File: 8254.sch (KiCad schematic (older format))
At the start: 4 parts, among them U18 PAL16L8, U19 8254

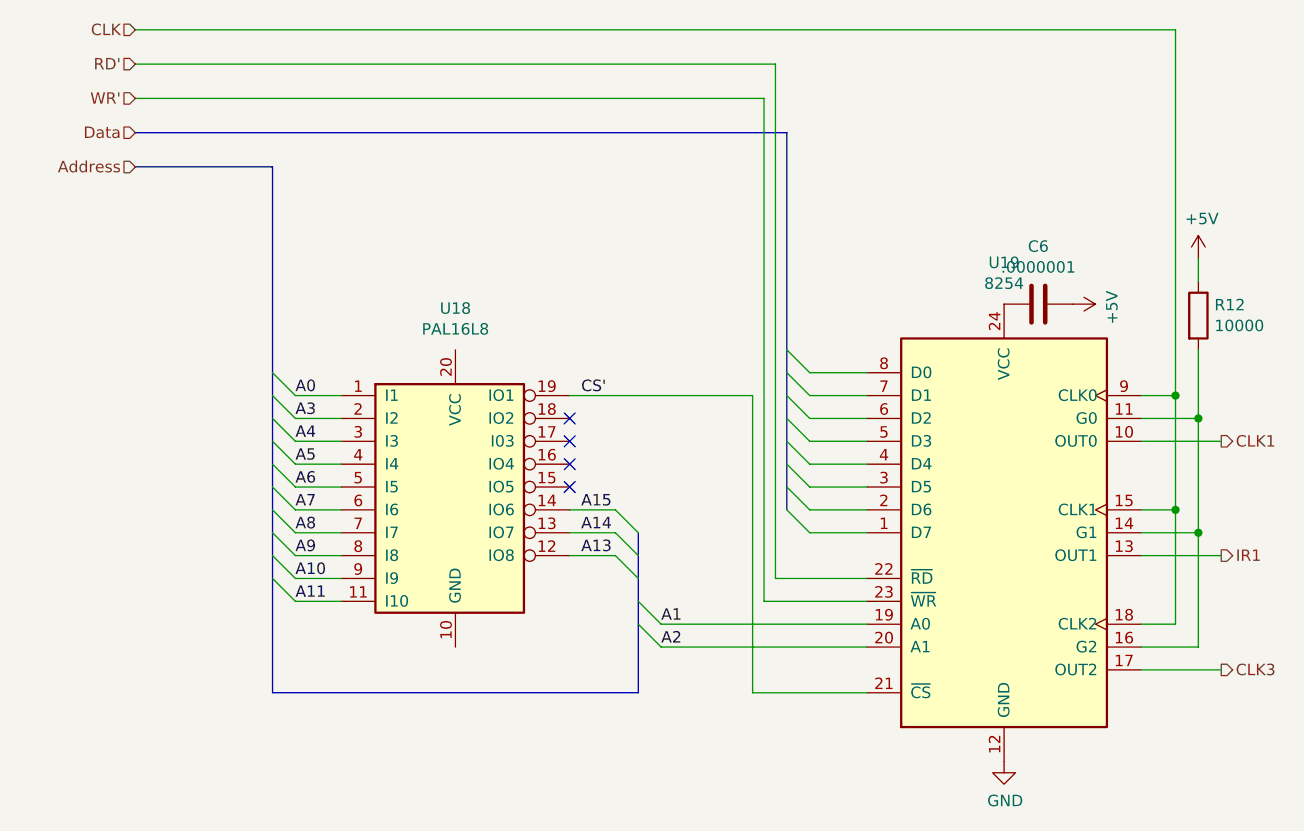
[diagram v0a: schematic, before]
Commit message: Integrated LCD.  Fixed issues with busses
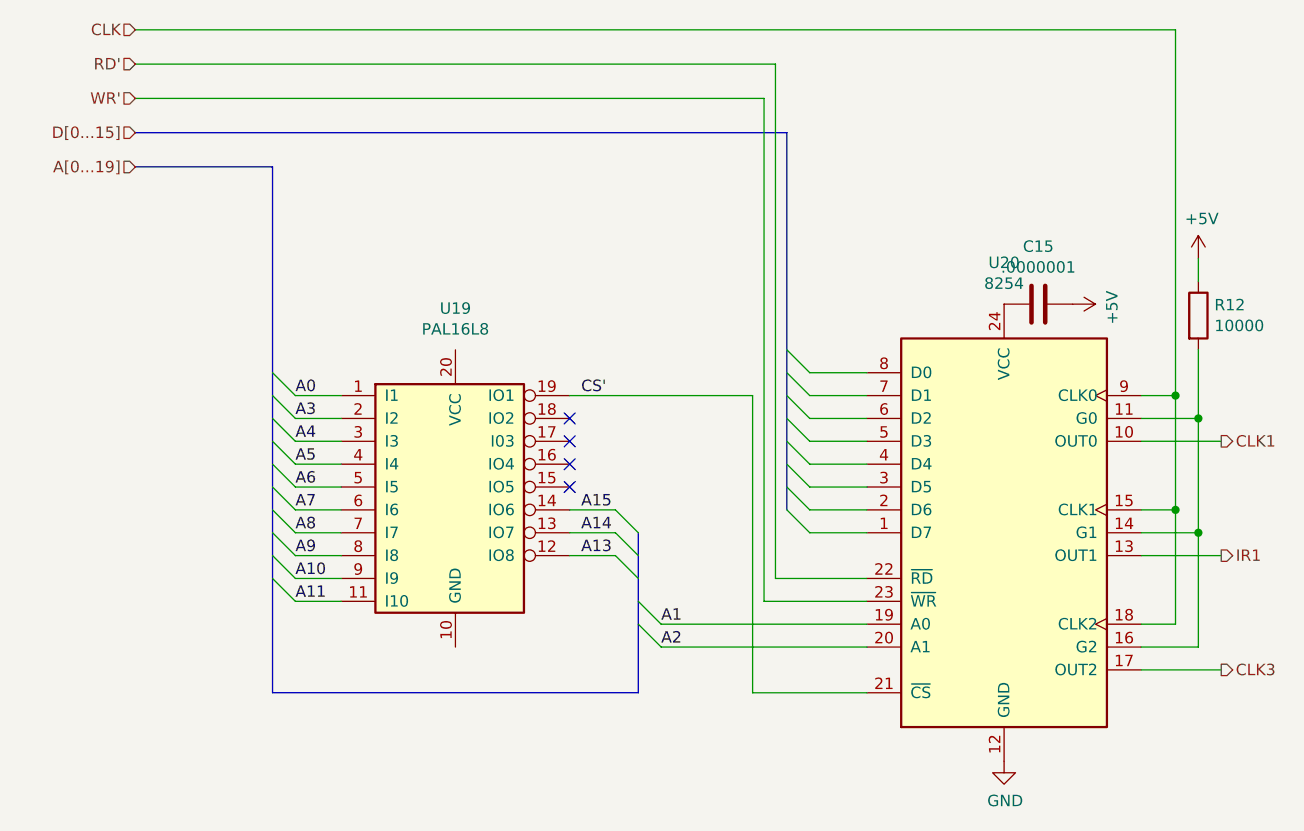
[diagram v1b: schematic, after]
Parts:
- renumbered C6 to C15, U18 to U19, U19 to U20
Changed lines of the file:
@@
 $Descr A4 11693 8268
 encoding utf-8
-Sheet 8 8
+Sheet 8 9
 Title ""
 Date ""
@@
 $EndDescr
 $Comp
-L Timer:8254 U19
+L Timer:8254 U20
 U 1 1 61B9DC78
 P 4950 3450
-F 0 "U19" H 4950 4631 50  0000 C CNN
+F 0 "U20" H 4950 4631 50  0000 C CNN
 F 1 "8254" H 4950 4540 50  0000 C CNN
 F 2 "Package_DIP:DIP-24_W15.24mm" H 5000 3700 50  0001 C CNN
@@
 $EndComp
 $Comp
-L power:+5V #PWR0112
+L power:+5V #PWR087
 U 1 1 61BA7924
 P 5250 2450
-F 0 "#PWR0112" H 5250 2300 50  0001 C CNN
+F 0 "#PWR087" H 5250 2300 50  0001 C CNN
 F 1 "+5V" H 5265 2623 50  0000 C CNN
 F 2 "" H 5250 2450 50  0001 C CNN
@@
 $EndComp
 $Comp
-L power:GND #PWR0113
+L power:GND #PWR086
 U 1 1 61BAD092
 P 4950 4450
-F 0 "#PWR0113" H 4950 4200 50  0001 C CNN
+F 0 "#PWR086" H 4950 4200 50  0001 C CNN
 F 1 "GND" H 4955 4277 50  0000 C CNN
 F 2 "" H 4950 4450 50  0001 C CNN
@@
 $EndComp
 $Comp
-L Logic_Programmable:PAL16L8 U18
+L Logic_Programmable:PAL16L8 U19
 U 1 1 61BB0CE0
 P 2550 3350
-F 0 "U18" H 2550 4231 50  0000 C CNN
+F 0 "U19" H 2550 4231 50  0000 C CNN
 F 1 "PAL16L8" H 2550 4140 50  0000 C CNN
 F 2 "" H 2550 3350 50  0001 C CNN
@@
 	1850 3750 2050 3750
 Text HLabel 1150 1700 0    50   Input ~ 0
-Data
+D[0...15]
 Text HLabel 1150 1850 0    50   Input ~ 0
-Address
+A[0...19]
 Wire Bus Line
 	1150 1700 4000 1700
@@
 	5700 2850 5700 3350
 $Comp
-L power:+5V #PWR0114
+L power:+5V #PWR088
 U 1 1 61BF17C5
 P 5800 2250
-F 0 "#PWR0114" H 5800 2100 50  0001 C CNN
+F 0 "#PWR088" H 5800 2100 50  0001 C CNN
 F 1 "+5V" H 5815 2423 50  0000 C CNN
 F 2 "" H 5800 2250 50  0001 C CNN
@@
 	3850 4150 4350 4150
 $Comp
-L Device:C C6
+L Device:C C15
 U 1 1 61C215F3
 P 5100 2450
-F 0 "C6" V 4848 2450 50  0000 C CNN
+F 0 "C15" V 4848 2450 50  0000 C CNN
 F 1 ".0000001" V 4939 2450 50  0000 C CNN
 F 2 "" H 5138 2300 50  0001 C CNN

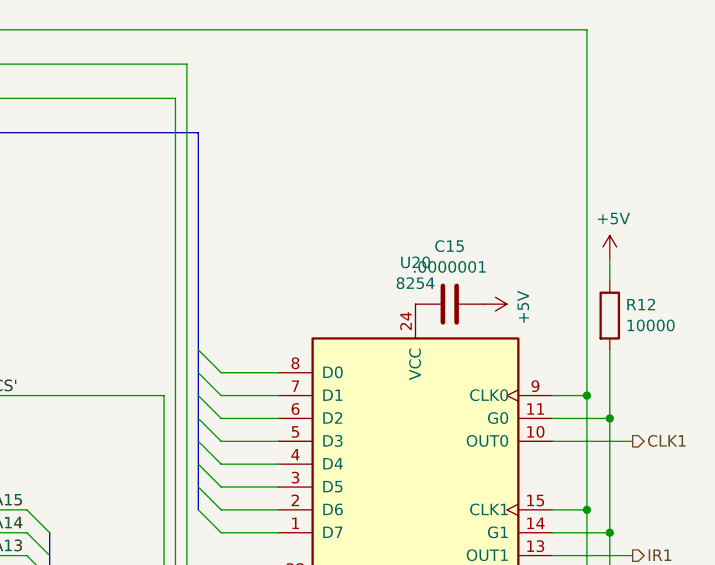
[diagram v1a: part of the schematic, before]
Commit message: All schematics present
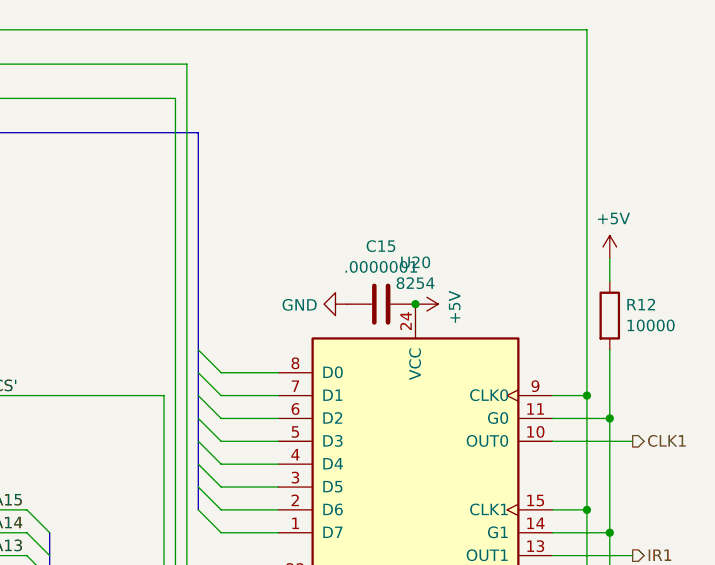
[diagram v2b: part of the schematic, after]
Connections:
- net +5V: now also U20.24 (VCC)
- net GND: now also C15.2
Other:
- moved on the sheet: C15
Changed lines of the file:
@@
 $Descr A4 11693 8268
 encoding utf-8
-Sheet 8 9
+Sheet 8 12
 Title ""
 Date ""
@@
 L power:+5V #PWR087
 U 1 1 61BA7924
-P 5250 2450
-F 0 "#PWR087" H 5250 2300 50  0001 C CNN
-F 1 "+5V" H 5265 2623 50  0000 C CNN
-F 2 "" H 5250 2450 50  0001 C CNN
-F 3 "" H 5250 2450 50  0001 C CNN
-	1    5250 2450
+P 4950 2450
+F 0 "#PWR087" H 4950 2300 50  0001 C CNN
+F 1 "+5V" H 4965 2623 50  0000 C CNN
+F 2 "" H 4950 2450 50  0001 C CNN
+F 3 "" H 4950 2450 50  0001 C CNN
+	1    4950 2450
 	0    1    1    0
 $EndComp
@@
 L Device:C C15
 U 1 1 61C215F3
-P 5100 2450
-F 0 "C15" V 4848 2450 50  0000 C CNN
-F 1 ".0000001" V 4939 2450 50  0000 C CNN
-F 2 "" H 5138 2300 50  0001 C CNN
-F 3 "~" H 5100 2450 50  0001 C CNN
-	1    5100 2450
+P 4800 2450
+F 0 "C15" V 4548 2450 50  0000 C CNN
+F 1 ".0000001" V 4639 2450 50  0000 C CNN
+F 2 "" H 4838 2300 50  0001 C CNN
+F 3 "~" H 4800 2450 50  0001 C CNN
+	1    4800 2450
 	0    1    1    0
 $EndComp
@@
 Wire Bus Line
 	1750 1850 1750 4150
+Connection ~ 4950 2450
+$Comp
+L power:GND #PWR0131
+U 1 1 61F867A8
+P 4650 2450
+F 0 "#PWR0131" H 4650 2200 50  0001 C CNN
+F 1 "GND" V 4655 2322 50  0000 R CNN
+F 2 "" H 4650 2450 50  0001 C CNN
+F 3 "" H 4650 2450 50  0001 C CNN
+	1    4650 2450
+	0    1    1    0
+$EndComp
 $EndSCHEMATC

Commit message: Started PCB
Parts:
- C35: renamed from C15; footprint (none) -> Capacitor_SMD:CP_Elec_3x5.3
- R30: renamed from R12; footprint (none) -> Resistor_SMD:R_0201_0603Metric
- U26: renamed from U19; footprint (none) -> Package_DIP:DIP-20_W7.62mm
- renumbered U20 to U27
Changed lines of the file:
@@
 $EndDescr
 $Comp
-L Timer:8254 U20
+L Timer:8254 U27
 U 1 1 61B9DC78
 P 4950 3450
-F 0 "U20" H 4950 4631 50  0000 C CNN
+F 0 "U27" H 4950 4631 50  0000 C CNN
 F 1 "8254" H 4950 4540 50  0000 C CNN
 F 2 "Package_DIP:DIP-24_W15.24mm" H 5000 3700 50  0001 C CNN
@@
 $EndComp
 $Comp
-L power:+5V #PWR087
+L power:+5V #PWR0121
 U 1 1 61BA7924
 P 4950 2450
-F 0 "#PWR087" H 4950 2300 50  0001 C CNN
+F 0 "#PWR0121" H 4950 2300 50  0001 C CNN
 F 1 "+5V" H 4965 2623 50  0000 C CNN
 F 2 "" H 4950 2450 50  0001 C CNN
@@
 $EndComp
 $Comp
-L power:GND #PWR086
+L power:GND #PWR0122
 U 1 1 61BAD092
 P 4950 4450
-F 0 "#PWR086" H 4950 4200 50  0001 C CNN
+F 0 "#PWR0122" H 4950 4200 50  0001 C CNN
 F 1 "GND" H 4955 4277 50  0000 C CNN
 F 2 "" H 4950 4450 50  0001 C CNN
@@
 $EndComp
 $Comp
-L Logic_Programmable:PAL16L8 U19
+L Logic_Programmable:PAL16L8 U26
 U 1 1 61BB0CE0
 P 2550 3350
-F 0 "U19" H 2550 4231 50  0000 C CNN
+F 0 "U26" H 2550 4231 50  0000 C CNN
 F 1 "PAL16L8" H 2550 4140 50  0000 C CNN
-F 2 "" H 2550 3350 50  0001 C CNN
+F 2 "Package_DIP:DIP-20_W7.62mm" H 2550 3350 50  0001 C CNN
 F 3 "" H 2550 3350 50  0001 C CNN
 	1    2550 3350
@@
 	5700 2850 5700 3350
 $Comp
-L power:+5V #PWR088
+L power:+5V #PWR0123
 U 1 1 61BF17C5
 P 5800 2250
-F 0 "#PWR088" H 5800 2100 50  0001 C CNN
+F 0 "#PWR0123" H 5800 2100 50  0001 C CNN
 F 1 "+5V" H 5815 2423 50  0000 C CNN
 F 2 "" H 5800 2250 50  0001 C CNN
@@
 $EndComp
 $Comp
-L Device:R R12
+L Device:R R30
 U 1 1 61BF2C82
 P 5800 2500
-F 0 "R12" H 5870 2546 50  0000 L CNN
+F 0 "R30" H 5870 2546 50  0000 L CNN
 F 1 "10000" H 5870 2455 50  0000 L CNN
-F 2 "" V 5730 2500 50  0001 C CNN
+F 2 "Resistor_SMD:R_0201_0603Metric" V 5730 2500 50  0001 C CNN
 F 3 "~" H 5800 2500 50  0001 C CNN
 	1    5800 2500
@@
 	3850 4150 4350 4150
 $Comp
-L Device:C C15
+L Device:C C35
 U 1 1 61C215F3
 P 4800 2450
-F 0 "C15" V 4548 2450 50  0000 C CNN
+F 0 "C35" V 4548 2450 50  0000 C CNN
 F 1 ".0000001" V 4639 2450 50  0000 C CNN
-F 2 "" H 4838 2300 50  0001 C CNN
+F 2 "Capacitor_SMD:CP_Elec_3x5.3" H 4838 2300 50  0001 C CNN
 F 3 "~" H 4800 2450 50  0001 C CNN
 	1    4800 2450
@@
 Text HLabel 5900 3550 2    50   Output ~ 0
 IR1
-Wire Bus Line
-	3350 3450 3350 4150
-Wire Bus Line
-	4000 1700 4000 3350
-Wire Bus Line
-	1750 1850 1750 4150
 Connection ~ 4950 2450
 $Comp
-L power:GND #PWR0131
+L power:GND #PWR0120
 U 1 1 61F867A8
 P 4650 2450
-F 0 "#PWR0131" H 4650 2200 50  0001 C CNN
+F 0 "#PWR0120" H 4650 2200 50  0001 C CNN
 F 1 "GND" V 4655 2322 50  0000 R CNN
 F 2 "" H 4650 2450 50  0001 C CNN
@@
 	0    1    1    0
 $EndComp
+Wire Bus Line
+	3350 3450 3350 4150
+Wire Bus Line
+	4000 1700 4000 3350
+Wire Bus Line
+	1750 1850 1750 4150
 $EndSCHEMATC
